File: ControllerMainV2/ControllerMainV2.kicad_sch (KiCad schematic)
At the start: 17 parts, among them J1 Conn_01x06, J2 Conn_01x10, J3 Conn_01x02, U11 74HC595, U17 74HC595

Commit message: Added libs
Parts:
- removed J3: Conn_01x02, Connector_JST:JST_PH_B2B-PH-K_1x02_P2.00mm_Vertical, symbol Connector_Generic:Conn_01x02
- removed U11, U17: 74HC595, SamacSys_Parts:SOIC127P600X175-16N, symbol 74xx:74HC595
- added U1, U2: MCP23009-E_SO, SamacSys_Parts:SOIC127P1030X265-18N, symbol SamacSys_Parts:MCP23009-E_SO
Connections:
- net EN is gone; now on net expr2: J2.1 (Pin_1)
- net SER_OE_N is gone; now on net expr1: J2.2 (Pin_2)
- net Ctrl1: now also U1.8 (GP0)
- net Ctrl2: now also U1.9 (GP1)
- net Ctrl3: now also U1.10 (GP2)
- net Ctrl4: now also U1.11 (GP3)
- net GND: now also U1.18 (VSS), U2.18 (VSS)
- net I2C_Reset: now also U1.6 (~{RESET}), U2.6 (~{RESET})
- net Mixer1_gain: now also U2.8 (GP0)
- net Mixer1_phi: now also U2.9 (GP1)
- net Mixer1_phi_n: now also U2.10 (GP2)
- net Mixer2_gain: now also U2.11 (GP3)
- net Mixer2_phi: now also U2.12 (GP4)
- net Mixer2_phi_n: now also U2.13 (GP5)
- net Out2_phi: now also U2.14 (GP6)
- net Out2_phi_n: now also U2.15 (GP7)
- net Outputs/Conn_Gnd: now also U1.12 (GP4)
- net SCL: now also U1.3 (SCL), U2.3 (SCL)
- net SDA: now also U1.4 (SDA), U2.4 (SDA)
- net Tuner: now also U1.13 (GP5)
- net VDD_3V3: now also U1.1 (VDD), U2.1 (VDD)
- net SER_Clk renamed RCLK
- net SER_Clr_N renamed CS
- net SER_In renamed EN_SPL
- net SER_Out renamed SCLK
- net SER_RClk renamed MOSI
- new net Addr6: U2.5 (ADDR)
- new net Addr7: U1.5 (ADDR)
- no-connect marks 2 -> 10
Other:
- sheet LoopJacks ports: added Addr6, Addr7; removed none
- sheet Outputs ports: added VDD_3V3; removed none
- sheet SwitchMatrix ports: added CS, EN_SPL_Matrix, MOSI, RCLK, SCLK, VDD_5V0; removed EN, SER_Clk, SER_Clr_N, SER_In, SER_OE_N, SER_Out, SER_RClk
- moved on the sheet: C_U11, C_U9

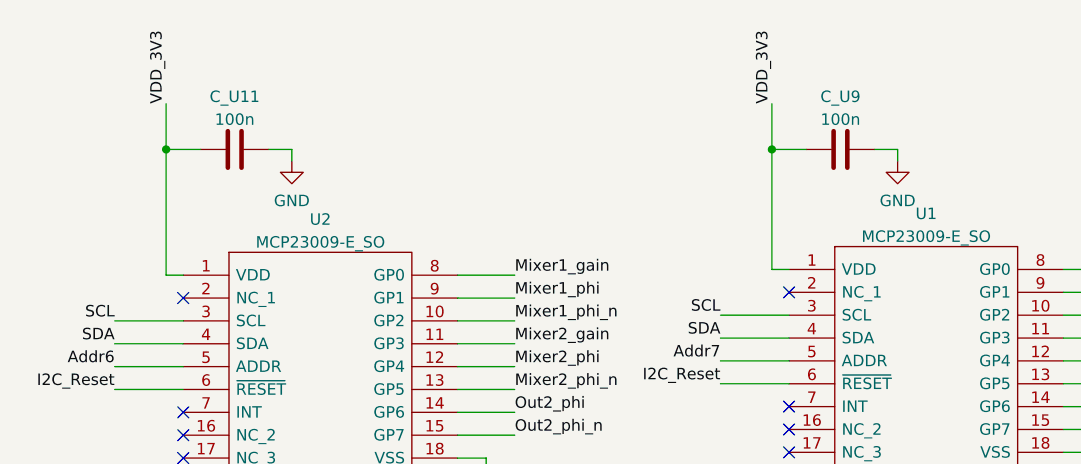
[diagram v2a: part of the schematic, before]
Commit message: Mixer, controll and supply wiring done. Matrix connections missing
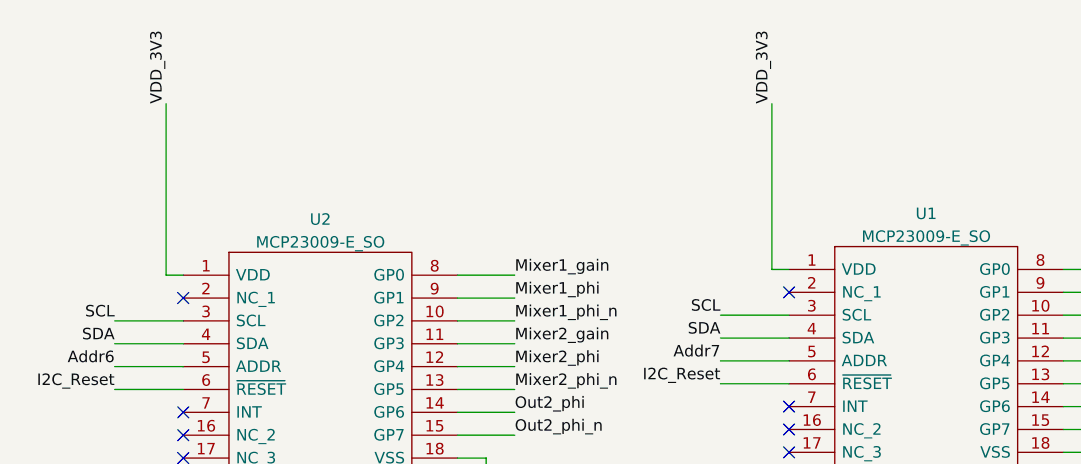
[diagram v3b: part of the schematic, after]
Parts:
- removed C_U11, C_U9: 100n, Capacitor_SMD:C_1206_3216Metric_Pad1.33x1.80mm_HandSolder, symbol Device:C
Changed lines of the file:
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@@
   (junction (at 181.61 101.6) (diameter 0) (color 0 0 0 0)
   )
-  (junction (at 347.345 26.67) (diameter 0) (color 0 0 0 0)
-  )
   (junction (at 181.61 99.06) (diameter 0) (color 0 0 0 0)
-  )
-  (junction (at 280.035 26.67) (diameter 0) (color 0 0 0 0)
   )
   (junction (at 95.25 67.31) (diameter 0) (color 0 0 0 0)
@@
     (stroke (width 0) (type default) (color 0 0 0 0))
   )
-  (wire (pts (xy 347.345 26.67) (xy 347.345 40.005))
-    (stroke (width 0) (type default) (color 0 0 0 0))
-  )
   (wire (pts (xy 243.84 88.9) (xy 247.65 88.9))
     (stroke (width 0) (type default) (color 0 0 0 0))
@@
     (stroke (width 0) (type default) (color 0 0 0 0))
   )
-  (wire (pts (xy 361.315 27.94) (xy 361.315 26.67))
-    (stroke (width 0) (type default) (color 0 0 0 0))
-  )
   (wire (pts (xy 241.3 142.24) (xy 241.3 148.59))
     (stroke (width 0) (type default) (color 0 0 0 0))
@@
     (stroke (width 0) (type default) (color 0 0 0 0))
   )
-  (wire (pts (xy 280.035 21.59) (xy 280.035 26.67))
-    (stroke (width 0) (type default) (color 0 0 0 0))
-  )
   (wire (pts (xy 249.555 179.07) (xy 249.555 184.15))
     (stroke (width 0) (type default) (color 0 0 0 0))
@@
     (stroke (width 0) (type default) (color 0 0 0 0))
   )
-  (wire (pts (xy 361.315 26.67) (xy 358.775 26.67))
-    (stroke (width 0) (type default) (color 0 0 0 0))
-  )
   (wire (pts (xy 107.95 67.31) (xy 107.95 63.5))
     (stroke (width 0) (type default) (color 0 0 0 0))
@@
     (stroke (width 0) (type default) (color 0 0 0 0))
   )
-  (wire (pts (xy 294.005 26.67) (xy 291.465 26.67))
-    (stroke (width 0) (type default) (color 0 0 0 0))
-  )
   (wire (pts (xy 219.71 157.48) (xy 215.9 157.48))
     (stroke (width 0) (type default) (color 0 0 0 0))
@@
     (stroke (width 0) (type default) (color 0 0 0 0))
   )
-  (wire (pts (xy 280.035 26.67) (xy 283.845 26.67))
-    (stroke (width 0) (type default) (color 0 0 0 0))
-  )
   (wire (pts (xy 346.71 130.81) (xy 186.69 130.81))
     (stroke (width 0) (type default) (color 0 0 0 0))
@@
     (stroke (width 0) (type default) (color 0 0 0 0))
   )
-  (wire (pts (xy 280.035 26.67) (xy 280.035 40.64))
+  (wire (pts (xy 280.035 21.59) (xy 280.035 40.64))
     (stroke (width 0) (type default) (color 0 0 0 0))
   )
@@
     (stroke (width 0) (type default) (color 0 0 0 0))
   )
-  (wire (pts (xy 347.345 21.59) (xy 347.345 26.67))
+  (wire (pts (xy 347.345 21.59) (xy 347.345 40.005))
     (stroke (width 0) (type default) (color 0 0 0 0))
   )
@@
     (stroke (width 0) (type default) (color 0 0 0 0))
   )
-  (wire (pts (xy 294.005 27.94) (xy 294.005 26.67))
-    (stroke (width 0) (type default) (color 0 0 0 0))
-  )
   (wire (pts (xy 186.69 104.14) (xy 191.77 104.14))
     (stroke (width 0) (type default) (color 0 0 0 0))
@@
   )
   (wire (pts (xy 341.63 50.165) (xy 349.25 50.165))
-    (stroke (width 0) (type default) (color 0 0 0 0))
-  )
-  (wire (pts (xy 347.345 26.67) (xy 351.155 26.67))
     (stroke (width 0) (type default) (color 0 0 0 0))
   )
@@
     )
     (property "Datasheet" "~" (id 3) (at 76.2 52.07 0)
-      (effects (font (size 1.27 1.27)) hide)
-    )
-    (pin "1")
-    (pin "2")
-  )
-  (symbol (lib_id "Device:C") (at 354.965 26.67 90) (unit 1)
-    (in_bom yes) (on_board yes) (fields_autoplaced)
-    (property "Reference" "C_U9" (id 0) (at 354.965 20.8112 90))
-    (property "Value" "100n" (id 1) (at 354.965 23.3481 90))
-    (property "Footprint" "Capacitor_SMD:C_1206_3216Metric_Pad1.33x1.80mm_HandSolder" (id 2) (at 358.775 25.7048 0)
-      (effects (font (size 1.27 1.27)) hide)
-    )
-    (property "Datasheet" "~" (id 3) (at 354.965 26.67 0)
       (effects (font (size 1.27 1.27)) hide)
     )
@@
     (pin "1")
   )
-  (symbol (lib_id "power:GND") (at 294.005 27.94 0) (unit 1)
-    (in_bom yes) (on_board yes) (fields_autoplaced)
-    (property "Reference" "#PWR015" (id 0) (at 294.005 34.29 0)
-      (effects (font (size 1.27 1.27)) hide)
-    )
-    (property "Value" "GND" (id 1) (at 294.005 32.3834 0))
-    (property "Footprint" "" (id 2) (at 294.005 27.94 0)
-      (effects (font (size 1.27 1.27)) hide)
-    )
-    (property "Datasheet" "" (id 3) (at 294.005 27.94 0)
-      (effects (font (size 1.27 1.27)) hide)
-    )
-    (pin "1")
-  )
   (symbol (lib_id "SamacSys_Parts:MCP23009-E_SO") (at 349.25 40.005 0) (unit 1)
     (in_bom yes) (on_board yes) (fields_autoplaced)
@@
     (pin "2")
   )
-  (symbol (lib_id "Device:C") (at 287.655 26.67 90) (unit 1)
-    (in_bom yes) (on_board yes) (fields_autoplaced)
-    (property "Reference" "C_U11" (id 0) (at 287.655 20.8112 90))
-    (property "Value" "100n" (id 1) (at 287.655 23.3481 90))
-    (property "Footprint" "Capacitor_SMD:C_1206_3216Metric_Pad1.33x1.80mm_HandSolder" (id 2) (at 291.465 25.7048 0)
-      (effects (font (size 1.27 1.27)) hide)
-    )
-    (property "Datasheet" "~" (id 3) (at 287.655 26.67 0)
-      (effects (font (size 1.27 1.27)) hide)
-    )
-    (pin "1")
-    (pin "2")
-  )
-  (symbol (lib_id "power:GND") (at 361.315 27.94 0) (unit 1)
-    (in_bom yes) (on_board yes) (fields_autoplaced)
-    (property "Reference" "#PWR077" (id 0) (at 361.315 34.29 0)
-      (effects (font (size 1.27 1.27)) hide)
-    )
-    (property "Value" "GND" (id 1) (at 361.315 32.3834 0))
-    (property "Footprint" "" (id 2) (at 361.315 27.94 0)
-      (effects (font (size 1.27 1.27)) hide)
-    )
-    (property "Datasheet" "" (id 3) (at 361.315 27.94 0)
-      (effects (font (size 1.27 1.27)) hide)
-    )
-    (pin "1")
-  )
   (symbol (lib_id "Mechanical:MountingHole") (at 127 24.13 0) (unit 1)
     (in_bom yes) (on_board yes) (fields_autoplaced)
@@
       (reference "#PWR01") (unit 1) (value "GND") (footprint "")
     )
+    (path "/00000000-0000-0000-0000-0000618cd10b/b947eca5-ba22-4d0c-8046-6c35d9969b65"
+      (reference "#PWR02") (unit 1) (value "GND") (footprint "")
+    )
     (path "/00000000-0000-0000-0000-0000618c6d5c/0d4de5b0-adbc-4ba9-9eab-1dd9b8b51ef6"
       (reference "#PWR03") (unit 1) (value "GND") (footprint "")
@@
       (reference "#PWR014") (unit 1) (value "GND") (footprint "")
     )
-    (path "/8ef15a91-4945-41e7-b0d0-efab3c60867a"
-      (reference "#PWR015") (unit 1) (value "GND") (footprint "")
-    )
     (path "/00000000-0000-0000-0000-0000618c6d5c/055adcc4-adcb-4cfa-9aff-fb5efeb69d70"
       (reference "#PWR016") (unit 1) (value "GND") (footprint "")
@@
       (reference "#PWR076") (unit 1) (value "GND") (footprint "")
     )
-    (path "/d501204c-4a1a-4795-8d20-a3bd93daf3d9"
-      (reference "#PWR077") (unit 1) (value "GND") (footprint "")
-    )
     (path "/96fedf5b-a5e1-40d9-8616-8018f29ca7bc/38f60618-14c7-4288-83ef-f9b4dcd5fa5c"
       (reference "#PWR078") (unit 1) (value "GND") (footprint "")
@@
       (reference "#PWR0127") (unit 1) (value "GND") (footprint "")
     )
+    (path "/00000000-0000-0000-0000-0000618cd10b/1f5db387-92a0-4bf6-9034-11f2272fc48b"
+      (reference "C1") (unit 1) (value "100n") (footprint "Capacitor_SMD:C_1206_3216Metric_Pad1.33x1.80mm_HandSolder")
+    )
+    (path "/00000000-0000-0000-0000-0000618cd10b/8b7b4ef6-6917-4928-88c3-20b753404009"
+      (reference "C2") (unit 1) (value "100n") (footprint "Capacitor_SMD:C_1206_3216Metric_Pad1.33x1.80mm_HandSolder")
+    )
     (path "/00000000-0000-0000-0000-0000618cd10b/00000000-0000-0000-0000-0000618ddbe1"
       (reference "C3") (unit 1) (value "100n") (footprint "Capacitor_SMD:C_1206_3216Metric_Pad1.33x1.80mm_HandSolder")
@@
       (reference "C_Spl8") (unit 1) (value "10u") (footprint "Capacitor_SMD:C_Elec_4x5.4")
     )
-    (path "/43670be0-aaf3-4c52-9ac2-c35f8c407ec4"
-      (reference "C_U9") (unit 1) (value "100n") (footprint "Capacitor_SMD:C_1206_3216Metric_Pad1.33x1.80mm_HandSolder")
-    )
-    (path "/cc28726c-9884-41e7-a23b-9c3ba01a0814"
-      (reference "C_U11") (unit 1) (value "100n") (footprint "Capacitor_SMD:C_1206_3216Metric_Pad1.33x1.80mm_HandSolder")
-    )
     (path "/96fedf5b-a5e1-40d9-8616-8018f29ca7bc/57ed4e00-afb5-46a6-975c-53e5a35ca6de"

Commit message: Changed main to 8 loop version. Might add buffers later
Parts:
- removed H2: MountingHole, MountingHole:MountingHole_3.2mm_M3, symbol Mechanical:MountingHole
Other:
- sheet LoopJacks ports: added none; removed Return1, Return2, Send1, Send2
